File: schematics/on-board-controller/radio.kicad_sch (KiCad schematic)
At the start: 2 parts, among them J1 5-1814832-1, U4 RFM98W-433S2

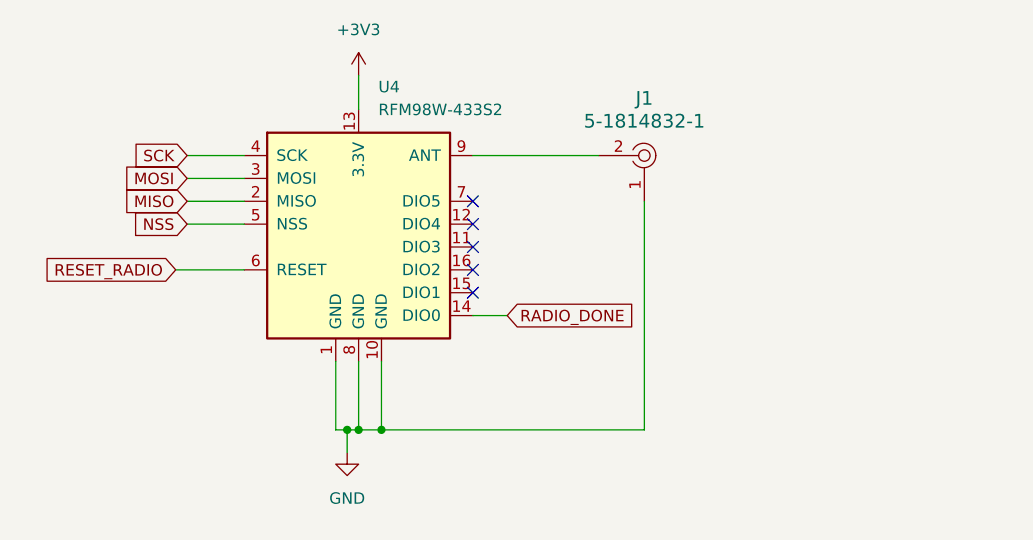
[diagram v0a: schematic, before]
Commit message: updated on-board schematic with changes
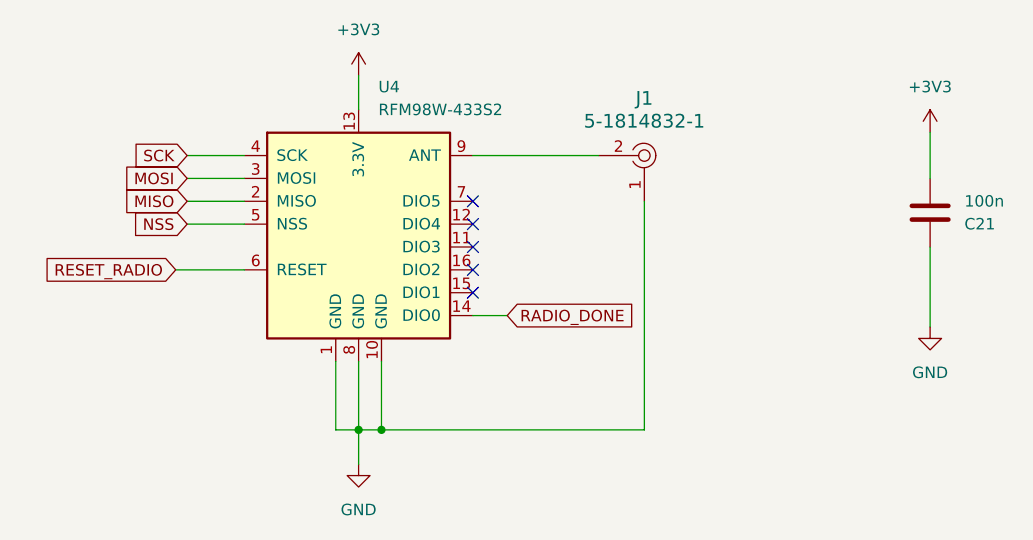
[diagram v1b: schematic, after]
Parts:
- added C21: 100n, Capacitor_SMD:C_0805_2012Metric_Pad1.18x1.45mm_HandSolder, symbol Device:C
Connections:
- net +3V3: now also C21.2
- net GND: now also C21.1
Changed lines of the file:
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@@
-		(color 0 0 0 0)
-	)
-	(junction
-		(at 138.43 106.68)
-		(diameter 0)
 		(color 0 0 0 0)
 	)
@@
 	(wire
 		(pts
-			(xy 138.43 109.22) (xy 138.43 106.68)
+			(xy 139.7 110.49) (xy 139.7 106.68)
 		)
 		(stroke
@@
 	(wire
 		(pts
-			(xy 138.43 106.68) (xy 139.7 106.68)
-		)
-		(stroke
-			(width 0)
-			(type default)
-		)
-	)
-	(wire
-		(pts
-			(xy 137.16 106.68) (xy 138.43 106.68)
+			(xy 203.2 95.25) (xy 203.2 86.36)
+		)
+		(stroke
+			(width 0)
+			(type default)
+		)
+	)
+	(wire
+		(pts
+			(xy 137.16 106.68) (xy 139.7 106.68)
 		)
 		(stroke
@@
 		(pts
 			(xy 137.16 99.06) (xy 137.16 106.68)
+		)
+		(stroke
+			(width 0)
+			(type default)
+		)
+	)
+	(wire
+		(pts
+			(xy 203.2 73.66) (xy 203.2 78.74)
 		)
 		(stroke
@@
 				(justify right)
 				(hide yes)
+			)
+		)
+	)
+	(symbol
+		(lib_id "Device:C")
+		(at 203.2 82.55 0)
+		(mirror x)
+		(unit 1)
+		(exclude_from_sim no)
+		(in_bom yes)
+		(on_board yes)
+		(dnp no)
+		(fields_autoplaced yes)
+		(property "Reference" "C21"
+			(at 207.01 83.8201 0)
+			(effects
+				(font
+					(size 1.27 1.27)
+				)
+				(justify left)
+			)
+		)
+		(property "Value" "100n"
+			(at 207.01 81.2801 0)
+			(effects
+				(font
+					(size 1.27 1.27)
+				)
+				(justify left)
+			)
+		)
+		(property "Footprint" "Capacitor_SMD:C_0805_2012Metric_Pad1.18x1.45mm_HandSolder"
+			(at 204.1652 78.74 0)
+			(effects
+				(font
+					(size 1.27 1.27)
+				)
+				(hide yes)
+			)
+		)
+		(property "Datasheet" "~"
+			(at 203.2 82.55 0)
+			(effects
+				(font
+					(size 1.27 1.27)
+				)
+				(hide yes)
+			)
+		)
+		(property "Description" "Unpolarized capacitor"
+			(at 203.2 82.55 0)
+			(effects
+				(font
+					(size 1.27 1.27)
+				)
+				(hide yes)
+			)
+		)
+		(pin "1"
+		)
+		(pin "2"
+		)
+		(instances
+			(project "sub"
+				(path "/aba2230e-80ca-41f8-a78f-a68ad044f9a5/9adeb370-0f8d-4058-9f16-ee34d985fe43"
+					(reference "C21")
+					(unit 1)
+				)
+			)
+		)
+	)
+	(symbol
+		(lib_id "power:+3V3")
+		(at 203.2 73.66 0)
+		(unit 1)
+		(exclude_from_sim no)
+		(in_bom yes)
+		(on_board yes)
+		(dnp no)
+		(fields_autoplaced yes)
+		(property "Reference" "#PWR036"
+			(at 203.2 77.47 0)
+			(effects
+				(font
+					(size 1.27 1.27)
+				)
+				(hide yes)
+			)
+		)
+		(property "Value" "+3V3"
+			(at 203.2 68.58 0)
+			(effects
+				(font
+					(size 1.27 1.27)
+				)
+			)
+		)
+		(property "Footprint" ""
+			(at 203.2 73.66 0)
+			(effects
+				(font
+					(size 1.27 1.27)
+				)
+				(hide yes)
+			)
+		)
+		(property "Datasheet" ""
+			(at 203.2 73.66 0)
+			(effects
+				(font
+					(size 1.27 1.27)
+				)
+				(hide yes)
+			)
+		)
+		(property "Description" "Power symbol creates a global label with name \"+3V3\""
+			(at 203.2 73.66 0)
+			(effects
+				(font
+					(size 1.27 1.27)
+				)
+				(hide yes)
+			)
+		)
+		(pin "1"
+		)
+		(instances
+			(project "sub"
+				(path "/aba2230e-80ca-41f8-a78f-a68ad044f9a5/9adeb370-0f8d-4058-9f16-ee34d985fe43"
+					(reference "#PWR036")
+					(unit 1)
+				)
 			)
 		)
@@
 	(symbol
 		(lib_id "power:GND")
-		(at 138.43 109.22 0)
+		(at 203.2 95.25 0)
 		(unit 1)
 		(exclude_from_sim no)
@@
 		(dnp no)
 		(fields_autoplaced yes)
+		(property "Reference" "#PWR037"
+			(at 203.2 101.6 0)
+			(effects
+				(font
+					(size 1.27 1.27)
+				)
+				(hide yes)
+			)
+		)
+		(property "Value" "GND"
+			(at 203.2 100.33 0)
+			(effects
+				(font
+					(size 1.27 1.27)
+				)
+			)
+		)
+		(property "Footprint" ""
+			(at 203.2 95.25 0)
+			(effects
+				(font
+					(size 1.27 1.27)
+				)
+				(hide yes)
+			)
+		)
+		(property "Datasheet" ""
+			(at 203.2 95.25 0)
+			(effects
+				(font
+					(size 1.27 1.27)
+				)
+				(hide yes)
+			)
+		)
+		(property "Description" "Power symbol creates a global label with name \"GND\" , ground"
+			(at 203.2 95.25 0)
+			(effects
+				(font
+					(size 1.27 1.27)
+				)
+				(hide yes)
+			)
+		)
+		(pin "1"
+		)
+		(instances
+			(project "sub"
+				(path "/aba2230e-80ca-41f8-a78f-a68ad044f9a5/9adeb370-0f8d-4058-9f16-ee34d985fe43"
+					(reference "#PWR037")
+					(unit 1)
+				)
+			)
+		)
+	)
+	(symbol
+		(lib_id "power:GND")
+		(at 139.7 110.49 0)
+		(unit 1)
+		(exclude_from_sim no)
+		(in_bom yes)
+		(on_board yes)
+		(dnp no)
+		(fields_autoplaced yes)
 		(property "Reference" "#PWR013"
-			(at 138.43 115.57 0)
+			(at 139.7 116.84 0)
 			(effects
 				(font
@@
 		)
 		(property "Value" "GND"
-			(at 138.43 114.3 0)
+			(at 139.7 115.57 0)
 			(effects
 				(font
@@
 		)
 		(property "Footprint" ""
-			(at 138.43 109.22 0)
+			(at 139.7 110.49 0)
 			(effects
 				(font
@@
 		)
 		(property "Datasheet" ""
-			(at 138.43 109.22 0)
+			(at 139.7 110.49 0)
 			(effects
 				(font
@@
 		)
 		(property "Description" "Power symbol creates a global label with name \"GND\" , ground"
-			(at 138.43 109.22 0)
-			(effects
-				(font
+			(at 139.7 110.49 0)
+			(effects
+				(font

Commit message: on-board: updated schematic to match STM32 confighuration
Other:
- title: sumbersible -> On-board Controller
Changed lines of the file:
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@@
 	(paper "A4")
 	(title_block
-		(title "sumbersible")
+		(title "On-board Controller")
 		(date "2024-07-16")
 		(rev "1")

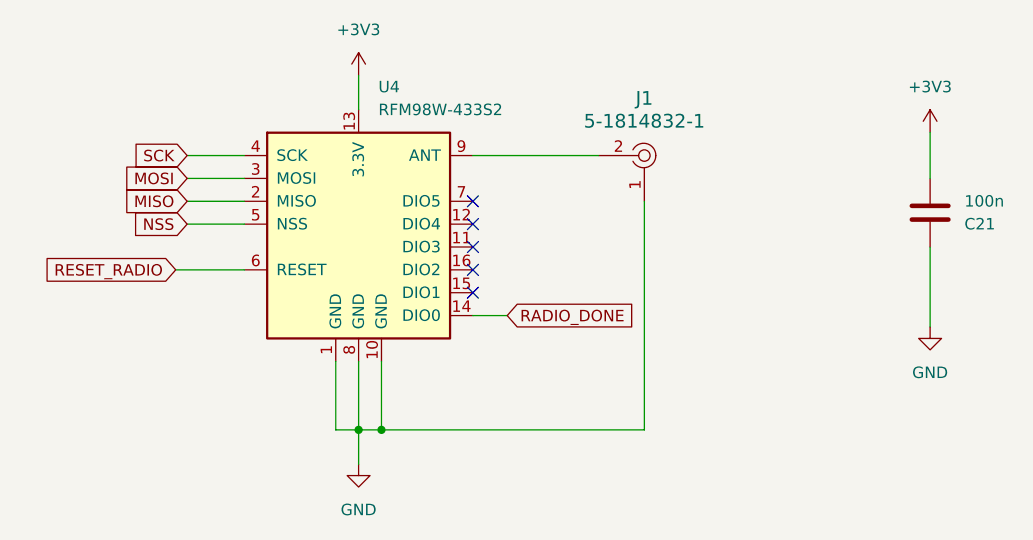
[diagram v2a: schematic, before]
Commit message: off-board: created schematic
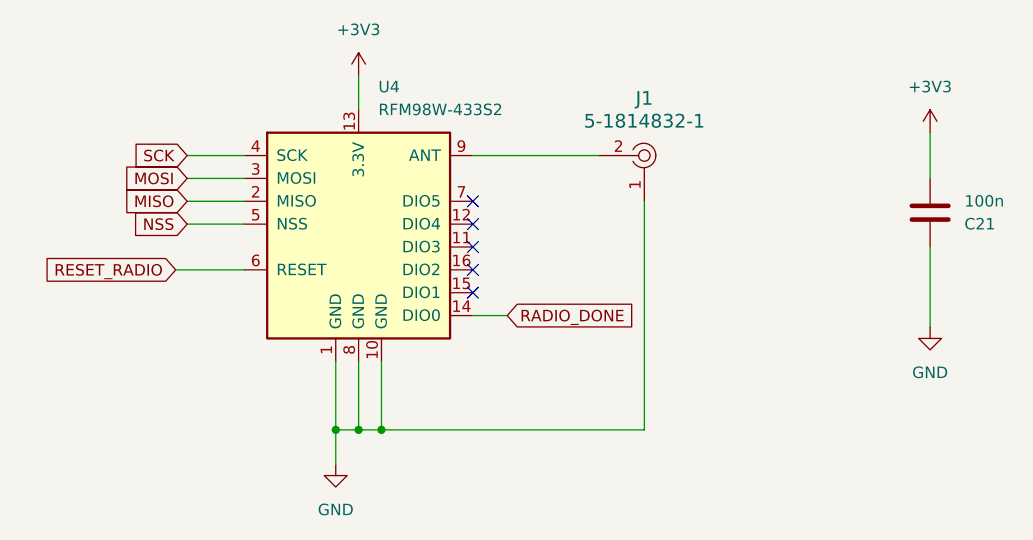
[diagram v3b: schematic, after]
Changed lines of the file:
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@@
+	)
+	(junction
+		(at 137.16 106.68)
+		(diameter 0)
+		(color 0 0 0 0)
 	)
 	(junction
@@
 	(wire
 		(pts
-			(xy 139.7 110.49) (xy 139.7 106.68)
+			(xy 137.16 110.49) (xy 137.16 106.68)
 		)
 		(stroke
@@
 	(symbol
 		(lib_id "power:GND")
-		(at 139.7 110.49 0)
+		(at 137.16 110.49 0)
 		(unit 1)
 		(exclude_from_sim no)
@@
 		(fields_autoplaced yes)
 		(property "Reference" "#PWR013"
-			(at 139.7 116.84 0)
+			(at 137.16 116.84 0)
 			(effects
 				(font
@@
 		)
 		(property "Value" "GND"
-			(at 139.7 115.57 0)
+			(at 137.16 115.57 0)
 			(effects
 				(font
@@
 		)
 		(property "Footprint" ""
-			(at 139.7 110.49 0)
+			(at 137.16 110.49 0)
 			(effects
 				(font
@@
 		)
 		(property "Datasheet" ""
-			(at 139.7 110.49 0)
+			(at 137.16 110.49 0)
 			(effects
 				(font
@@
 		)
 		(property "Description" "Power symbol creates a global label with name \"GND\" , ground"
-			(at 139.7 110.49 0)
-			(effects
-				(font
+			(at 137.16 110.49 0)
+			(effects
+				(font
